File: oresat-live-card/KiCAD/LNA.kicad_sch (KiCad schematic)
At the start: 32 parts, among them J12 Conn_Coaxial, J14 Conn_01x02, U18 TQP3M9037, U27 PAT1220-C-3DB, U28 PD2328J5050S2HF, U29 LTC5538

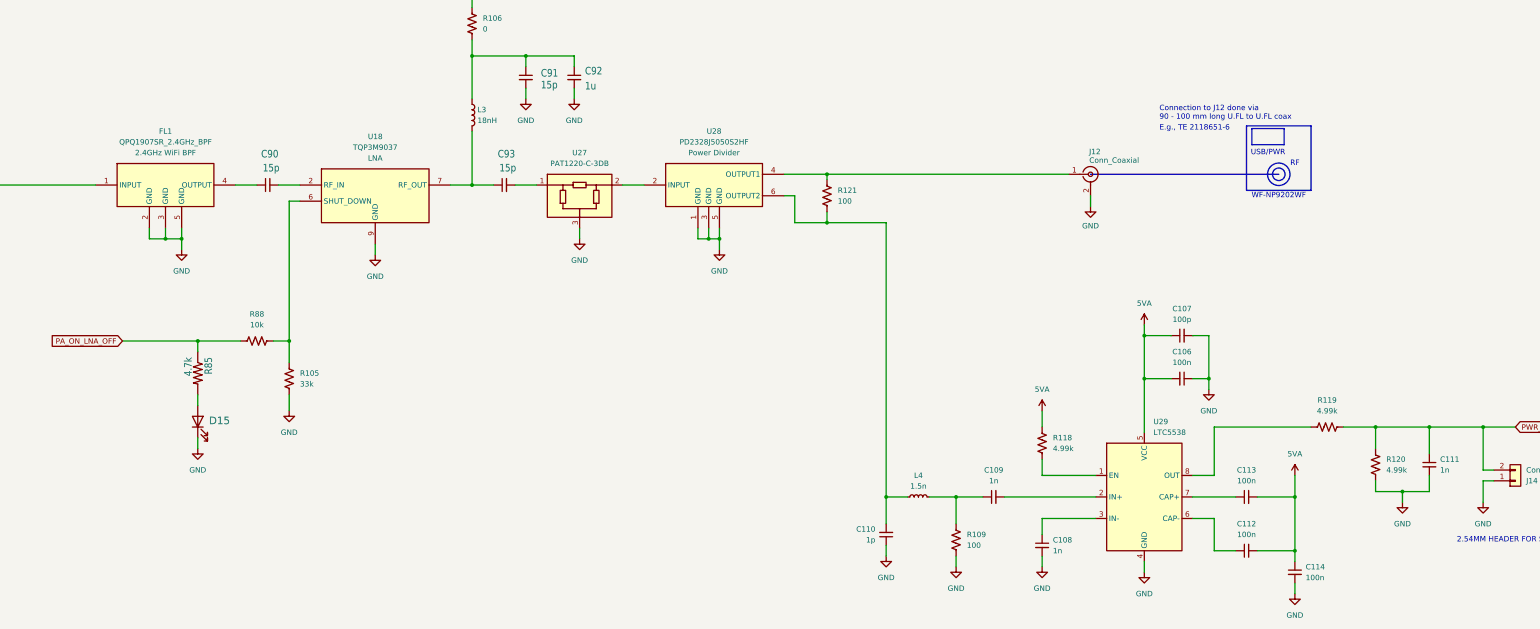
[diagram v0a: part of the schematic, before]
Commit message: Fixed up schematic as best as possible. There were a lot of issues with local paths being referenced, and EAGLE import libraries. Fixed all of those, as well as fixed some oresat-kicad IC symbols (bad direction pins) and I think we're now OK. Also updated card outline for two RF (LEFT) connectors.  Still missing two packages, but we'll deal with that later.
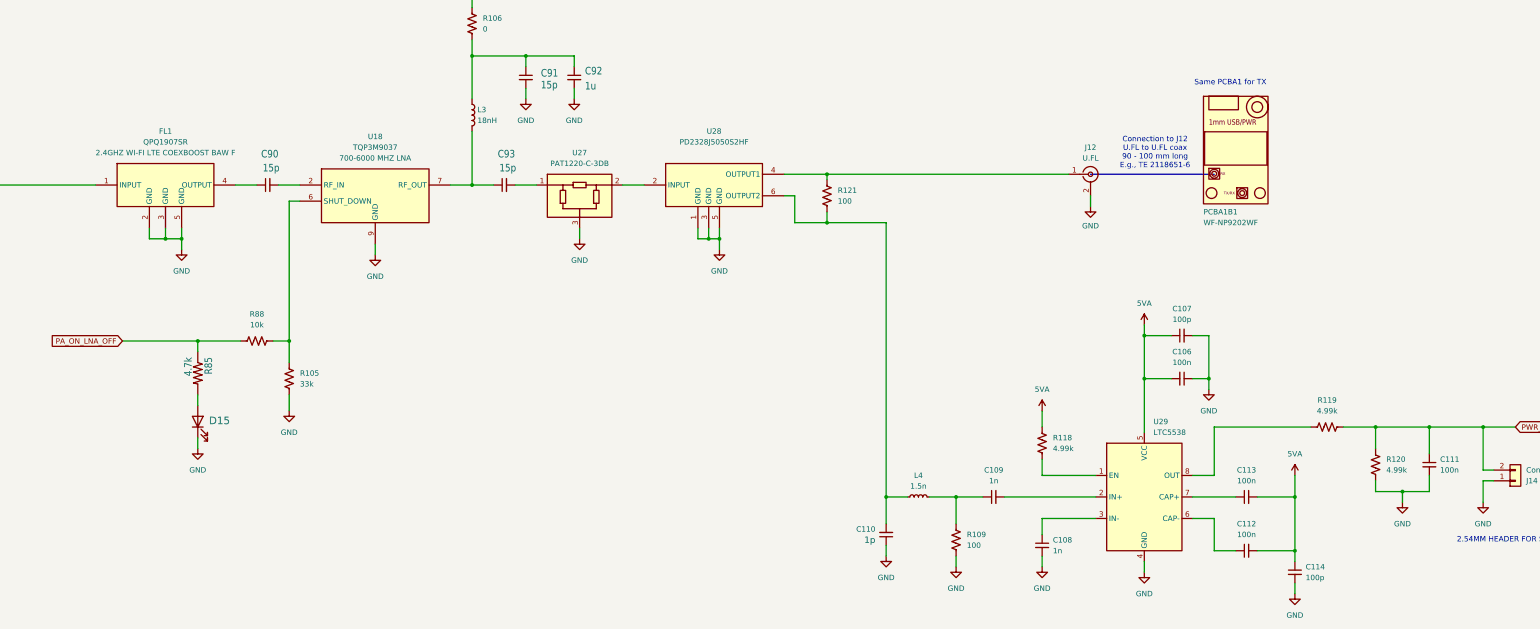
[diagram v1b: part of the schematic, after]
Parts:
- added PCBA1B1: WF-NP9202WF, symbol oresat-pcbs:WF-NP9202WF
- C106, C112, C113: footprint (none) -> Resistor_SMD:R_0603_1608Metric; DPN (none) -> 445-5667-1-ND; Distributor (none) -> DigiKey; MFR (none) -> TDK Corporation; MPN (none) -> CGA3E2X7R1E104K080AA
- C107: footprint (none) -> Resistor_SMD:R_0402_1005Metric; DPN (none) -> 490-GCM1555C1H101GA16DCT-ND; Distributor (none) -> DigiKey; MFR (none) -> Murata Electronics; MPN (none) -> GCM1555C1H101GA16D
- C108, C109: footprint (none) -> Resistor_SMD:R_0402_1005Metric; DPN (none) -> 445-12118-1-ND; Distributor (none) -> DigiKey; MFR (none) -> TDK Corporation; MPN (none) -> CGA2B2NP01H102J050BA
- C110: footprint (none) -> Resistor_SMD:R_0402_1005Metric; DPN (none) -> 490-17745-1-ND; Distributor (none) -> DigiKey; MFR (none) -> Murata Electronics; MPN (none) -> GCM1555C1H1R0CA16J
- C111: value 1n -> 100n; footprint (none) -> Resistor_SMD:R_0603_1608Metric; DPN (none) -> 445-5667-1-ND; Distributor (none) -> DigiKey; MFR (none) -> TDK Corporation; MPN (none) -> CGA3E2X7R1E104K080AA
- C114: value 100n -> 100p; footprint (none) -> Resistor_SMD:R_0402_1005Metric; DPN (none) -> 490-GCM1555C1H101GA16DCT-ND; Distributor (none) -> DigiKey; MFR (none) -> Murata Electronics; MPN (none) -> GCM1555C1H101GA16D
- C92: footprint oresat-passives:0603-C-NOSILK -> Resistor_SMD:R_0603_1608Metric; DPN 445-173717-1-ND -> 445-12539-1-ND; MPN CGA3E1X7R1E105M080AE -> CGA3E1X7R1C105K080AC
- D15: value 150060VS55040 -> GREEN; DPN (none) -> 732-150060GS75020CT-ND; MFR (none) -> Würth Elektronik
- FL1: value QPQ1907SR_2.4GHz_BPF -> QPQ1907SR; footprint QPQ1907SR -> (none); DPN (none) -> 2312-QPQ1907SRCT-ND; Distributor (none) -> DigiKey; Height 0.975 -> (none)
- J12: value Conn_Coaxial -> U.FL; DPN (none) -> H11891CT-ND; Distributor (none) -> DigiKey; MFR (none) -> Hirose Electric Co Ltd; MPN (none) -> U.FL-R-SMT-1(10)
- J14: footprint (none) -> Connector_PinHeader_2.54mm:PinHeader_1x02_P2.54mm_Vertical
- L4: footprint (none) -> Resistor_SMD:R_0402_1005Metric; DPN (none) -> 2035-1382-1-ND; Distributor (none) -> DigiKey; MFR (none) -> Delta Electronics/Components; MPN (none) -> 0402HM-1N5EKTS
- R105: footprint (none) -> Resistor_SMD:R_0603_1608Metric; DPN (none) -> 10-ERJ-U03F3302VCT-ND; Distributor (none) -> DigiKey; MFR (none) -> Panasonic; MPN (none) -> ERJ-U03F3302V
- R106: footprint (none) -> Resistor_SMD:R_0603_1608Metric; DPN (none) -> P0.0GCT-ND; Distributor (none) -> DigiKey; MFR (none) -> Panasonic; MPN (none) -> ERJ-3GEY0R00V
- R109, R121: footprint (none) -> Resistor_SMD:R_0603_1608Metric; DPN (none) -> P100HCT-ND; Distributor (none) -> DigiKey; MFR (none) -> Panasonic; MPN (none) -> ERJ-3EKF1000V
- R118, R119, R120: footprint (none) -> Resistor_SMD:R_0603_1608Metric; DPN (none) -> P4.99KHCT-ND; Distributor (none) -> DigiKey; MFR (none) -> Panasonic; MPN (none) -> ERJ-3EKF4991V
- R85: DPN (none) -> ERJ-3EKF4701V; MFR (none) -> Panasonic; MPN ERJ-3EKF1002V -> ERJ-3EKF4701V
- R88: footprint (none) -> Resistor_SMD:R_0603_1608Metric; DPN (none) -> P10.0KHCT-ND; Distributor (none) -> DigiKey; MFR (none) -> Panasonic; MPN (none) -> ERJ-3EKF1002V
- U18: DPN (none) -> 2312-TQP3M9037CT-ND; Distributor (none) -> DigiKey; Height 0.95 -> (none); Mouser Part Number 772-TQP3M9037 -> (none); Mouser Price/Stock https://www.mouser.co.uk/ProductDetail/Qorvo/TQP3M9037?qs=7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 -> (none)
- U27: DPN (none) -> PAT123CT-ND; Distributor (none) -> DigiKey; MFR (none) -> Susumu; MPN (none) -> PAT1220-C-3DB-T5
- U28: DPN (none) -> 1173-1098-1-ND; Distributor (none) -> DigiKey; Height 0.58 -> (none); MFR ANAREN -> Anaren; Mouser Part Number 620-PD2328J5050S2HF -> (none); Mouser Price/Stock https://www.mouser.co.uk/ProductDetail/Anaren/PD2328J5050S2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 -> (none)
- U29: DPN (none) -> LT5538IDD#TRPBFCT-ND; Distributor (none) -> DigiKey; MFR (none) -> Analog Devices; MPN (none) -> LT5538IDD#TRPBF
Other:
- note added: "Connection to J12 U.FL to U.FL coax 90 - 100 mm long E.g., TE 2118651-6"
- note added: "Same PCBA1 for TX"
- note removed: "Connection to J12 done via 90 - 100 mm long U.FL to U.FL coax"
- note removed: "E.g., TE 2118651-6"
- note removed: "RF"
- note removed: "USB/PWR"
- note removed: "WF-NP9202WF"

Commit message: updated sheet numbering and title, merged antenna switching and tx rx switching sheets
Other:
- title: (none) -> Oresat DxWifi Card
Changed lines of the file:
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@@
 	(paper "B")
 	(title_block
-		(date "2025-05-28")
+		(title "Oresat DxWifi Card")
+		(date "2025-07-06")
 		(rev "2")
 	)

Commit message: Removed or-gate U6 and jumper J5, added Tx/Rx timing delay graphic to schematic, updated all symbols from oresat library, added new components to PCB and started grouping them
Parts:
- U18: Height (none) -> 0.95; Mouser Part Number (none) -> 772-TQP3M9037; Mouser Price/Stock (none) -> https://www.mouser.co.uk/ProductDetail/Qorvo/TQP3M9037?qs=7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
- U28: footprint PD2328J5050S2HF -> oresat-misc:PD2328J5050S2HF; Height (none) -> 0.58; MFR Anaren -> ANAREN; Mouser Part Number (none) -> 620-PD2328J5050S2HF; Mouser Price/Stock (none) -> https://www.mouser.co.uk/ProductDetail/Anaren/PD2328J5050S2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
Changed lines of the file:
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@@
+			)
+		)
+		(property "Height" "0.95"
+			(at 139.7 454.61 0)
+			(effects
+				(font
+					(size 1.27 1.27)
+				)
+				(justify left top)
+				(hide yes)
+			)
+		)
+		(property "Mouser Part Number" "772-TQP3M9037"
+			(at 139.7 754.61 0)
+			(effects
+				(font
+					(size 1.27 1.27)
+				)
+				(justify left top)
+				(hide yes)
+			)
+		)
+		(property "Mouser Price/Stock" "https://www.mouser.co.uk/ProductDetail/Qorvo/TQP3M9037?qs=73ok1p1Z9vsY6%252BSqiDpCeg%3D%3D"
+			(at 139.7 854.61 0)
+			(effects
+				(font
+					(size 1.27 1.27)
+				)
+				(justify left top)
+				(hide yes)
+			)
+		)
+		(property "Arrow Part Number" ""
+			(at 139.7 954.61 0)
+			(effects
+				(font
+					(size 1.27 1.27)
+				)
+				(justify left top)
+				(hide yes)
+			)
+		)
+		(property "Arrow Price/Stock" ""
+			(at 139.7 1054.61 0)
+			(effects
+				(font
+					(size 1.27 1.27)
+				)
+				(justify left top)
+				(hide yes)
 			)
 		)
@@
 			)
 		)
-		(property "Footprint" "PD2328J5050S2HF"
+		(property "Footprint" "oresat-misc:PD2328J5050S2HF"
 			(at 218.44 168.58 0)
 			(effects
@@
 			)
 		)
-		(property "Description" "RF POWER DVDR 2.3GHZ-2.8GHZ 0805"
+		(property "Description" "Power Divider 50ohm 2300 - 2800 MHz"
 			(at 205.74 68.58 0)
 			(effects
@@
 			)
 		)
-		(property "MFR" "Anaren "
+		(property "MFR" "ANAREN"
 			(at 218.44 568.58 0)
 			(effects
@@
 				(hide yes)
 			)
+		)
+		(property "Height" "0.58"
+			(at 218.44 468.58 0)
+			(effects
+				(font
+					(size 1.27 1.27)
+				)
+				(justify left top)
+				(hide yes)
+			)
+		)
+		(property "Mouser Part Number" "620-PD2328J5050S2HF"
+			(at 218.44 768.58 0)
+			(effects
+				(font
+					(size 1.27 1.27)
+				)
+				(justify left top)
+				(hide yes)
+			)
+		)
+		(property "Mouser Price/Stock" "https://www.mouser.co.uk/ProductDetail/Anaren/PD2328J5050S2HF?qs=61pwXRo0i5ghxO%2FqzA2OdA%3D%3D"
+			(at 218.44 868.58 0)
+			(effects
+				(font
+					(size 1.27 1.27)
+				)
+				(justify left top)
+				(hide yes)
+			)

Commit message: Changed C118, R124, R125 from 0603 to 0402, starting layout and routing
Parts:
- U18: footprint SON50P200X200X95-9N-D -> Package_DFN_QFN:DFN-8-1EP_2x2mm_P0.5mm_EP0.8x1.6mm
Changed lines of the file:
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@@
 			)
 		)
-		(property "Footprint" "SON50P200X200X95-9N-D"
+		(property "Footprint" "Package_DFN_QFN:DFN-8-1EP_2x2mm_P0.5mm_EP0.8x1.6mm"
 			(at 139.7 154.61 0)
 			(effects

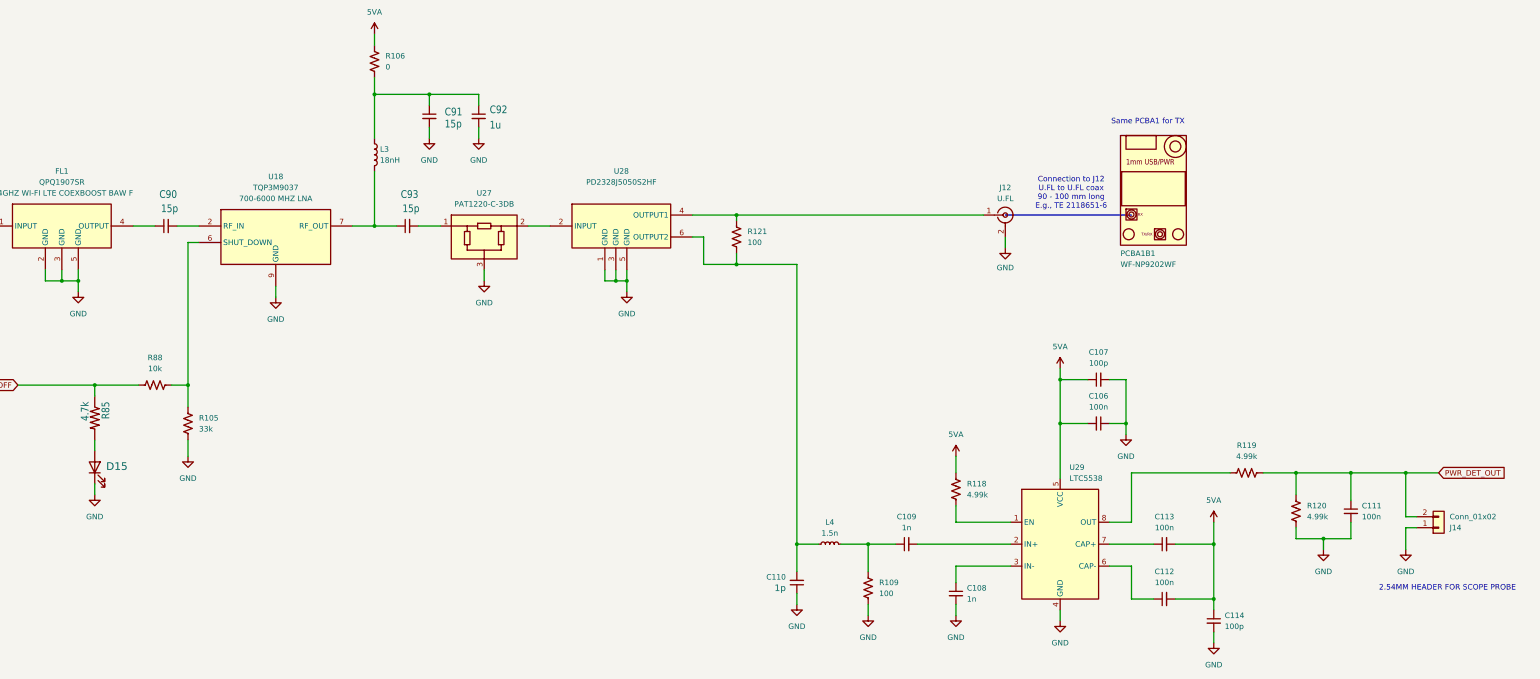
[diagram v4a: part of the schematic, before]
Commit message: added notes to schematic, added footprints to Fl1 & U29 & U23,35, updated changes to board
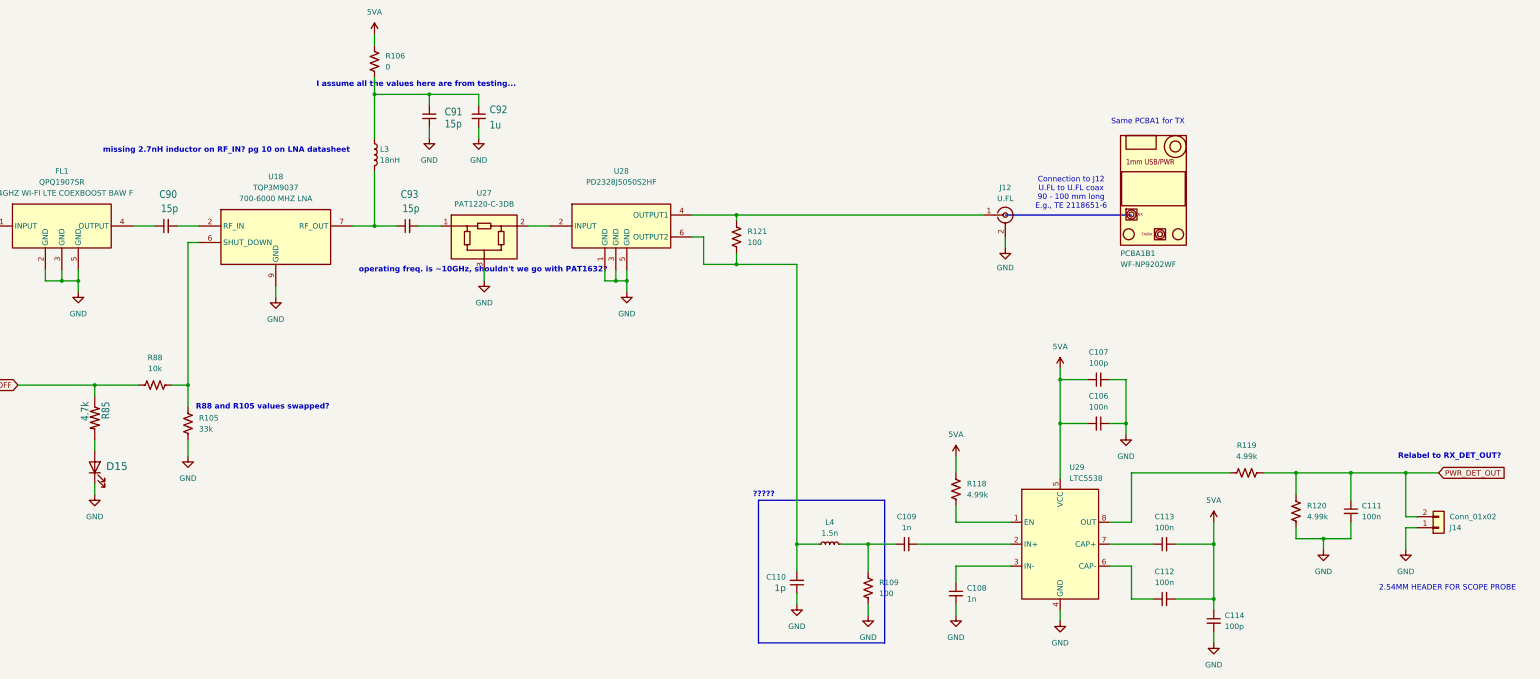
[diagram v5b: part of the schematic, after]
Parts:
- FL1: footprint (none) -> oresat-ics:QPQ1907SR
- U29: footprint (none) -> Package_DFN_QFN:DFN-8-1EP_3x3mm_P0.5mm_EP1.65x2.38mm
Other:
- note added: "?????"
- note added: "I assume all the values here are from testing..."
- note added: "R88 and R105 values swapped?"
- note added: "Relabel to RX_DET_OUT?"
- note added: "missing 2.7nH inductor on RF_IN? pg 10 on LNA datasheet"
- note added: "operating freq. is ~10GHz, shouldn't we go with PAT1632?"
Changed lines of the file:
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@@
 		(rev "2")
 	)
+	(rectangle
+		(start 237.49 139.7)
+		(end 266.7 172.72)
+		(stroke
+			(width 0)
+			(type default)
+		)
+		(fill
+			(type none)
+		)
+	)
+	(text "I assume all the values here are from testing..."
+		(exclude_from_sim no)
+		(at 158.242 43.434 0)
+		(effects
+			(font
+				(size 1.27 1.27)
+				(thickness 0.254)
+				(bold yes)
+			)
+		)
+	)
 	(text "Same PCBA1 for TX"
 		(exclude_from_sim no)
@@
 		)
 	)
+	(text "missing 2.7nH inductor on RF_IN? pg 10 on LNA datasheet"
+		(exclude_from_sim no)
+		(at 114.3 58.674 0)
+		(effects
+			(font
+				(size 1.27 1.27)
+				(thickness 0.254)
+				(bold yes)
+			)
+		)
+	)
+	(text "operating freq. is ~10GHz, shouldn't we go with PAT1632?"
+		(exclude_from_sim no)
+		(at 173.736 86.36 0)
+		(effects
+			(font
+				(size 1.27 1.27)
+				(thickness 0.254)
+				(bold yes)
+			)
+		)
+	)
 	(text "2.54MM HEADER FOR SCOPE PROBE"
 		(exclude_from_sim no)
@@
 		)
 	)
+	(text "?????"
+		(exclude_from_sim no)
+		(at 238.7267 138.3976 0)
+		(effects
+			(font
+				(size 1.27 1.27)
+				(thickness 0.254)
+				(bold yes)
+			)
+		)
+	)
+	(text "R88 and R105 values swapped?"
+		(exclude_from_sim no)
+		(at 122.682 118.11 0)
+		(effects
+			(font
+				(size 1.27 1.27)
+				(thickness 0.254)
+				(bold yes)
+			)
+		)
+	)
+	(text "Relabel to RX_DET_OUT?"
+		(exclude_from_sim no)
+		(at 397.51 129.54 0)
+		(effects
+			(font
+				(size 1.27 1.27)
+				(thickness 0.254)
+				(bold yes)
+			)
+		)
+	)
 	(text "Connection to J12\nU.FL to U.FL coax\n90 - 100 mm long \nE.g., TE 2118651-6"
 		(exclude_from_sim no)
@@
 		)
 	)
+	(table
+		(column_count 2)
+		(border
+			(external yes)
+			(header yes)
+			(stroke
+				(width 0)
+				(type solid)
+			)
+		)
+		(separators
+			(rows yes)
+			(cols yes)
+			(stroke
+				(width 0)
+				(type solid)
+			)
+		)
+		(column_widths 17.78 19.05)
+		(row_heights 3.175 3.175 3.175)
+		(cells
+			(table_cell "LNA SHUTDOWN"
+				(exclude_from_sim no)
+				(at 106.68 101.6 0)
+				(size 17.78 3.175)
+				(margins 0.9525 0.9525 0.9525 0.9525)
+				(span 1 1)
+				(fill
+					(type none)
+				)
+				(effects
+					(font
+						(size 1.27 1.27)
+					)
+					(justify left top)
+				)
+			)
+			(table_cell ""
+				(exclude_from_sim no)
+				(at 124.46 101.6 0)
+				(size 19.05 3.175)
+				(margins 0.9525 0.9525 0.9525 0.9525)
+				(span 1 1)
+				(fill
+					(type none)
+				)
+				(effects
+					(font
+						(size 1.27 1.27)
+					)
+					(justify left top)
+				)
+			)
+			(table_cell "ON"
+				(exclude_from_sim no)
+				(at 106.68 104.775 0)
+				(size 17.78 3.175)
+				(margins 0.9525 0.9525 0.9525 0.9525)
+				(span 1 1)
+				(fill
+					(type none)
+				)
+				(effects
+					(font
+						(size 1.27 1.27)
+					)
+					(justify left top)
+				)
+			)
+			(table_cell "(0, x, 0.4) V"
+				(exclude_from_sim no)
+				(at 124.46 104.775 0)
+				(size 19.05 3.175)
+				(margins 0.9525 0.9525 0.9525 0.9525)
+				(span 1 1)
+				(fill
+					(type none)
+				)
+				(effects
+					(font
+						(size 1.27 1.27)
+					)
+					(justify left top)
+				)
+			)
+			(table_cell "OFF"
+				(exclude_from_sim no)
+				(at 106.68 107.95 0)
+				(size 17.78 3.175)
+				(margins 0.9525 0.9525 0.9525 0.9525)
+				(span 1 1)
+				(fill
+					(type none)
+				)
+				(effects
+					(font
+						(size 1.27 1.27)
+					)
+					(justify left top)
+				)
+			)
+			(table_cell "(2.5, 3.3, VDD) V"
+				(exclude_from_sim no)
+				(at 124.46 107.95 0)
+				(size 19.05 3.175)
+				(margins 0.9525 0.9525 0.9525 0.9525)
+				(span 1 1)
+				(fill
+					(type none)
+				)
+				(effects
+					(font
+						(size 1.27 1.27)
+					)
+					(justify left top)
+				)
+			)
+		)
+	)
 	(global_label "PWR_DET_OUT"
 		(shape input)
@@
 			)
 		)
-		(property "Footprint" ""
+		(property "Footprint" "Package_DFN_QFN:DFN-8-1EP_3x3mm_P0.5mm_EP1.65x2.38mm"
 			(at 307.34 149.86 0)
 			(effects
@@
 			)
 		)
-		(property "Datasheet" ""
+		(property "Datasheet" "https://www.analog.com/media/en/technical-documentation/data-sheets/5538f.pdf"
 			(at 307.34 149.86 0)
 			(effects
@@
 			)
 		)
-		(property "Footprint" ""
+		(property "Footprint" "oresat-ics:QPQ1907SR"
 			(at 88.9 168.58 0)
 			(effects
